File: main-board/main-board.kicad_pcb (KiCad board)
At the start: 2 copper layers, 180 x 111 mm, 53 parts, among them J1 INPUT, J2 NC1, J3 OUTPUT, J4 Conn_01x03_Pin, J5 COM, J6 Conn_01x03_Pin, SW1 SW_SPST, U1 ADA4898-2, U2 ADA4898-2, U3 AD633ANZ

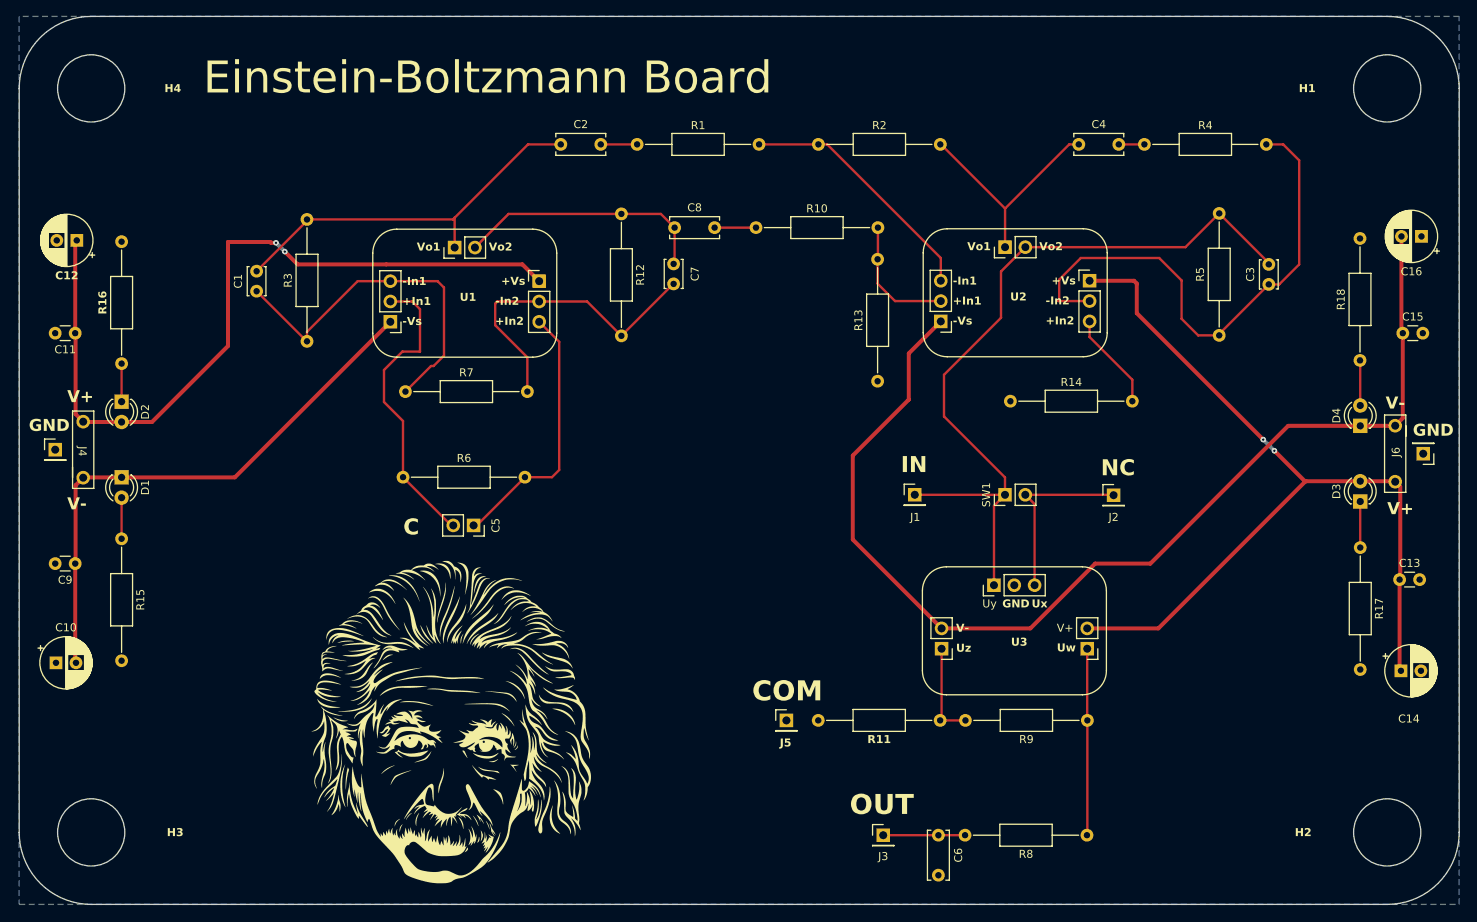
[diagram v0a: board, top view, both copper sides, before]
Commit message: Change M8 Holes to M5 Holes
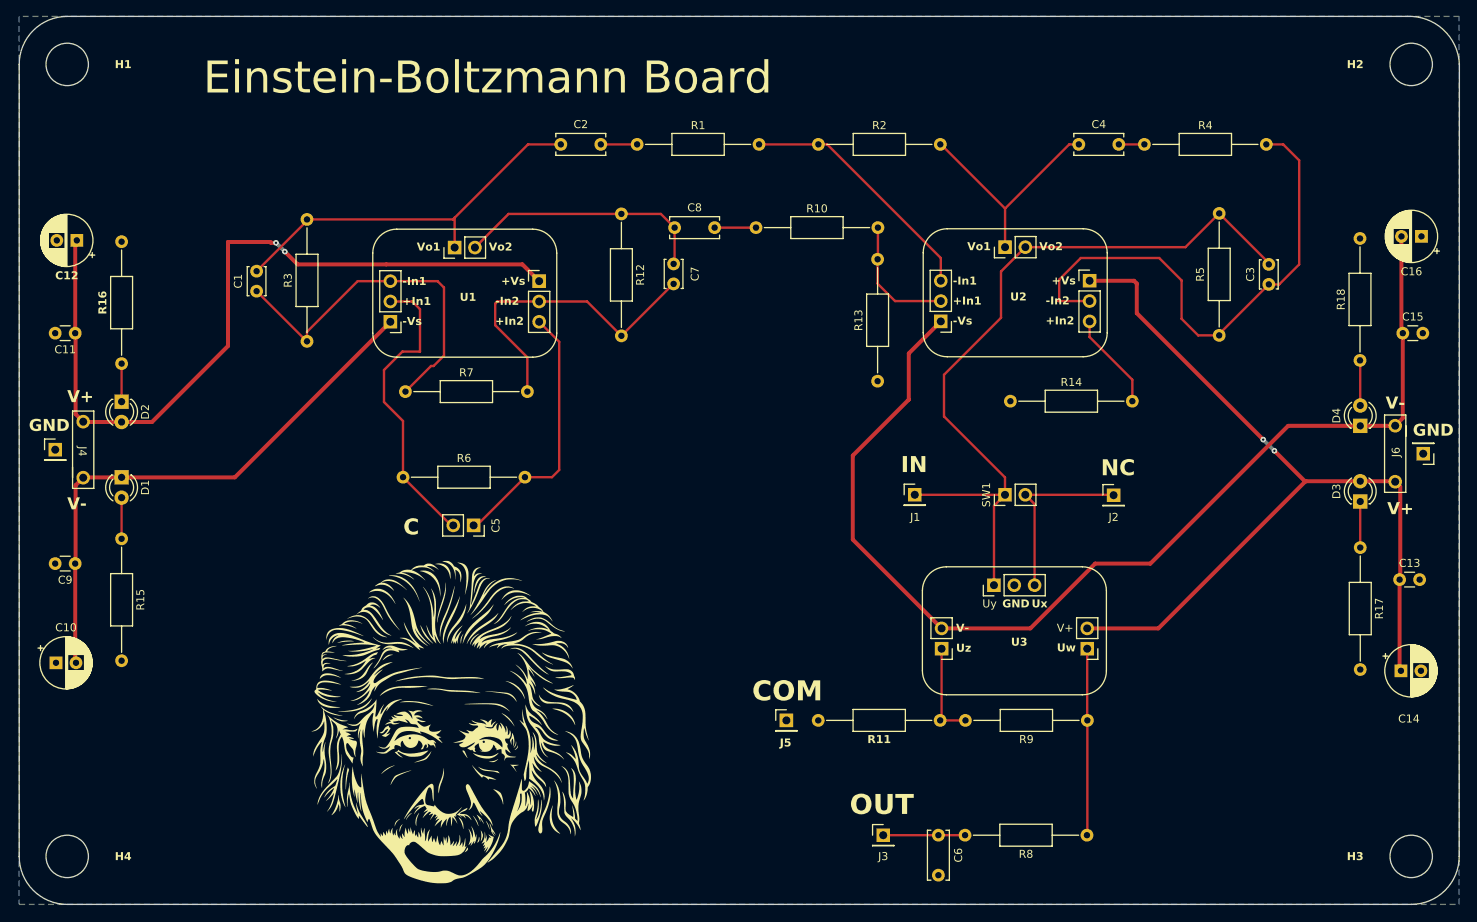
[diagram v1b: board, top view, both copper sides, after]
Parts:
- H1, H2, H3, H4: footprint MountingHole:MountingHole_8.4mm_M8 -> MountingHole:MountingHole_5.3mm_M5
- moved H1 165.0 mm to (66.0, 49.0)
- moved H3 165.0 mm to (234.0, 148.0)
- moved H2 96.0 mm to (234.0, 49.0)
- moved H4 96.0 mm to (66.0, 148.0)
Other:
- outline, holes or cut-outs redrawn

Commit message: Changes capacitor and resistor footprints
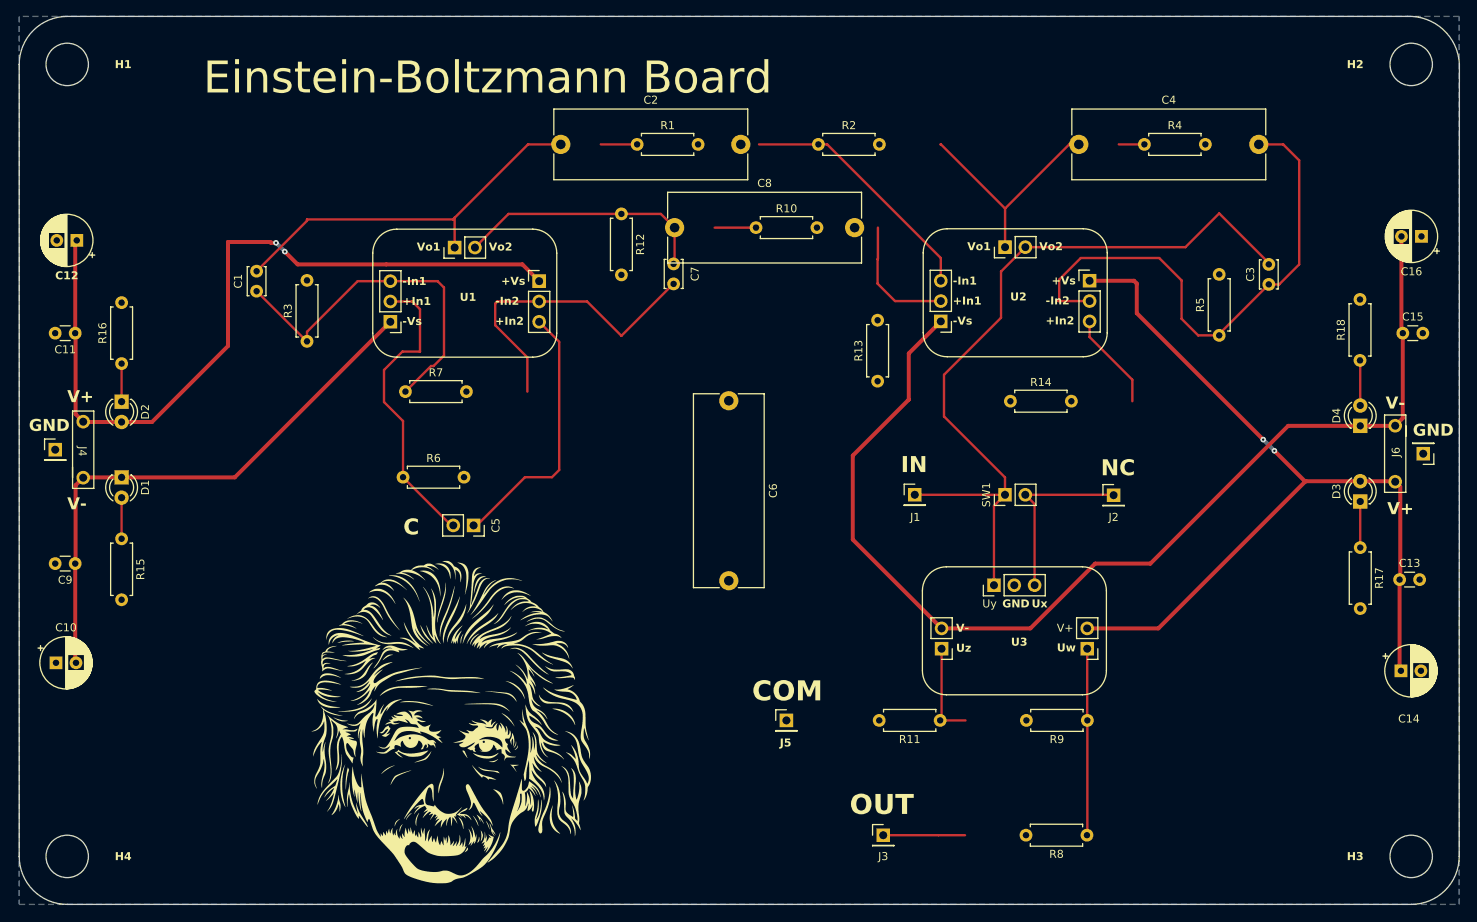
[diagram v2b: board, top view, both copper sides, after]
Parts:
- C2, C4, C6, C8: footprint Capacitor_THT:C_Disc_D6.0mm_W2.5mm_P5.00mm -> Capacitor_THT:C_Rect_L24.0mm_W8.6mm_P22.50mm_MKT
- R1, R10, R11, R12, R13, R14, R15, R16, R17, R18, R2, R3, R4, R5, R6, R7, R8, R9: footprint Resistor_THT:R_Axial_DIN0207_L6.3mm_D2.5mm_P15.24mm_Horizontal -> Resistor_THT:R_Axial_DIN0207_L6.3mm_D2.5mm_P7.62mm_Horizontal
- moved C6 60.3 mm to (148.7, 91.0)

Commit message: Saves progress
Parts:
- J1, J2, J3, J5: footprint Connector_PinHeader_2.54mm:PinHeader_1x01_P2.54mm_Vertical -> footprints:Banana_Jack_1Pin
- moved J1 96.2 mm to (84.4, 142.5)
- moved J3 84.5 mm to (85.8, 126.1)
- moved J2 26.6 mm to (213.6, 123.5)
- moved J5 18.0 mm to (140.0, 122.7)
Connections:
- C1 pad 2: /w3 -> VCC
- C2 pad 1: /w3 -> VCC
- U1 pad 4: /w3 -> VCC
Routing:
- net /w3: track 48.4 -> 0.00 mm
- net VCC: track 99.1 -> 146.0 mm, vias 2 -> 0
- net /w_out: track 10.2 -> 0.00 mm

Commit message: Adds Switch footprint and 3d model
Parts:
- added SW2: SW_Push_SPDT, footprints:Switch_Toggle_SPDT_SS12F46, F.Cu at (88.4, 104.4)
- added SW3: SW_Push_SPDT, footprints:Switch_Toggle_SPDT_SS12F46, F.Cu at (96.0, 104.4)
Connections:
- C1 pad 2: VCC -> /w3
- C2 pad 1: VCC -> /w3
- U1 pad 4: VCC -> /w3
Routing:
- net VCC: track 146.0 -> 97.6 mm
- net /w3: track 0.00 -> 48.4 mm

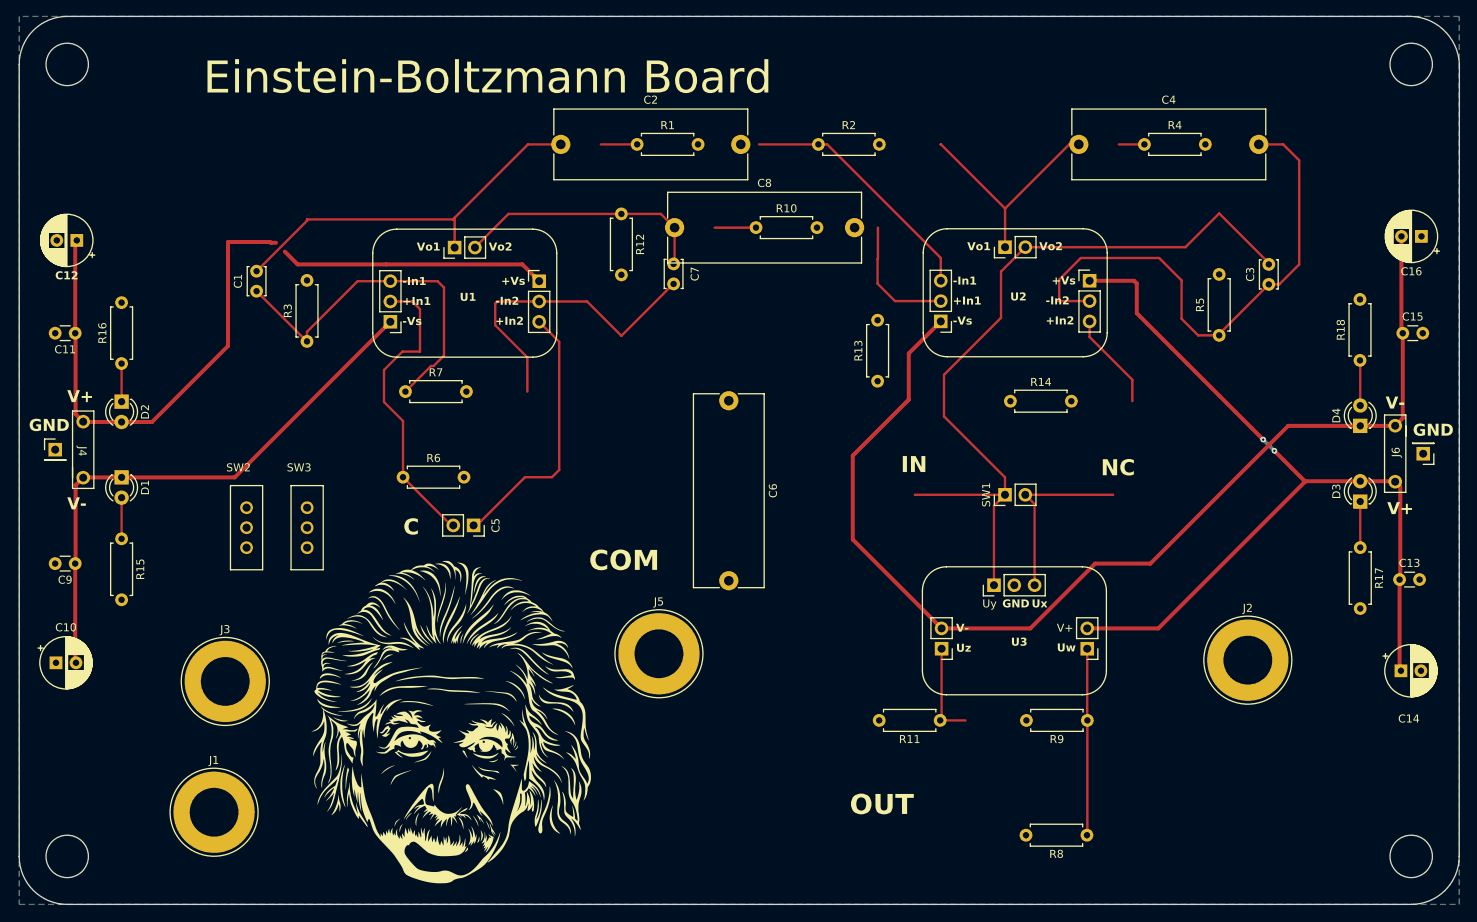
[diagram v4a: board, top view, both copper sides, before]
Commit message: Solves the 4 batteries problem
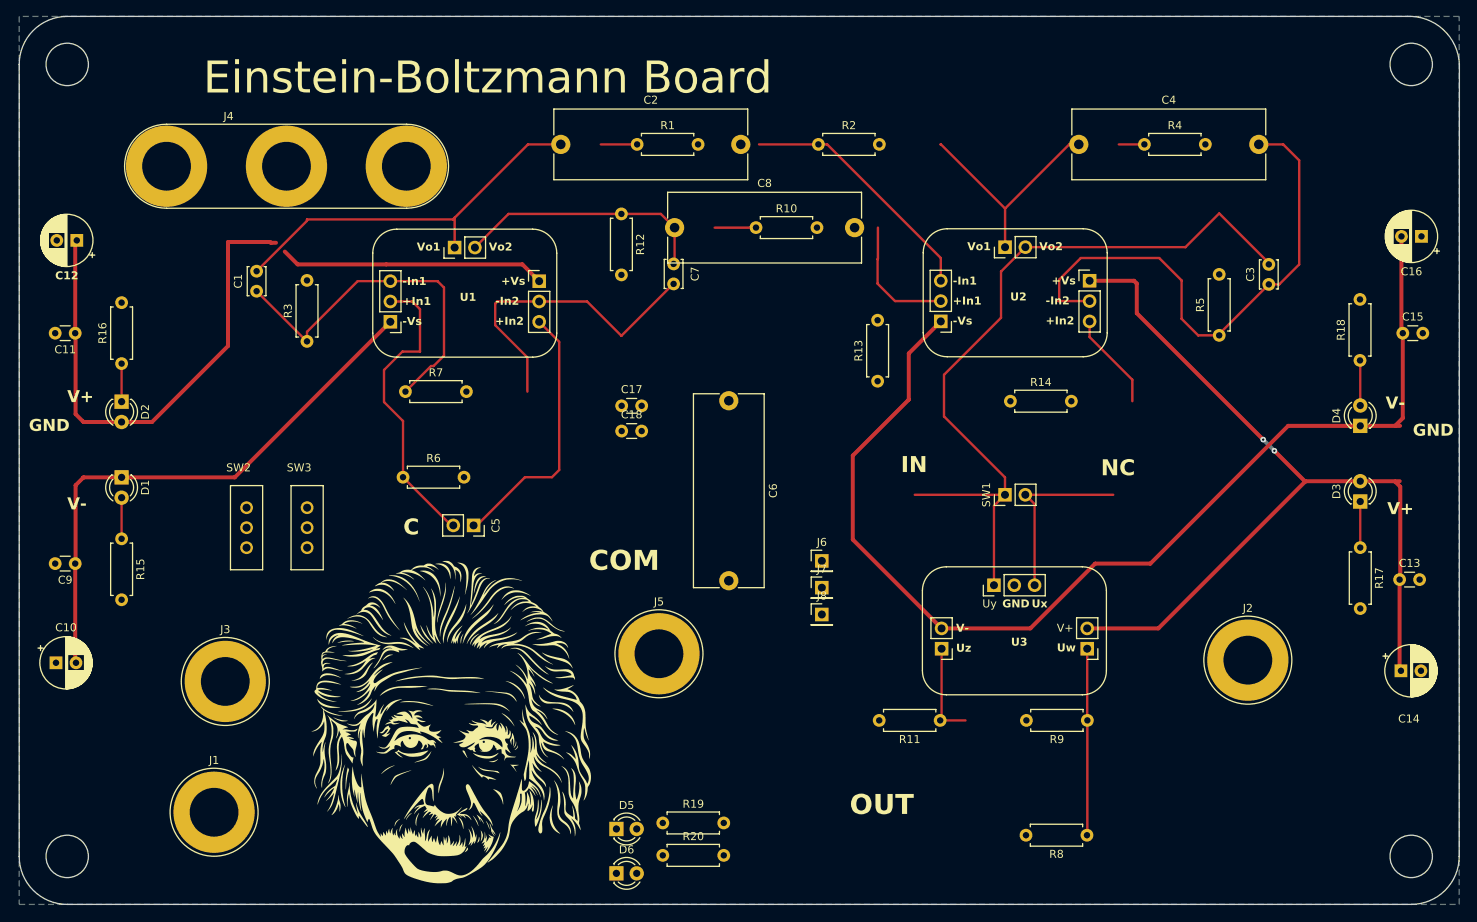
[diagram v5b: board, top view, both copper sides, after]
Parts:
- added C17: 0.1u, Capacitor_THT:C_Disc_D3.0mm_W1.6mm_P2.50mm, F.Cu at (135.3, 91.7)
- added C18: 0.1u, Capacitor_THT:C_Disc_D3.0mm_W1.6mm_P2.50mm, F.Cu at (135.3, 94.8)
- added D5: LED, LED_THT:LED_D3.0mm, F.Cu at (134.7, 144.6)
- added D6: LED, LED_THT:LED_D3.0mm, F.Cu at (134.7, 150.1)
- added J7: NC__DEBUG, Connector_PinHeader_2.54mm:PinHeader_1x01_P2.54mm_Vertical, F.Cu at (160.3, 114.4)
- added J8: OUTPUT_DEBUG, Connector_PinHeader_2.54mm:PinHeader_1x01_P2.54mm_Vertical, F.Cu at (160.3, 117.8)
- added R19: 2k, Resistor_THT:R_Axial_DIN0207_L6.3mm_D2.5mm_P7.62mm_Horizontal, F.Cu at (140.4, 143.8)
- added R20: 2k, Resistor_THT:R_Axial_DIN0207_L6.3mm_D2.5mm_P7.62mm_Horizontal, F.Cu at (140.4, 147.9)
- J4: footprint footprints:PowerHeader -> footprints:Banana_Jack_3Pin
- J6: value Conn_01x03_Pin -> INPUT_DEBUG; footprint footprints:PowerHeader -> Connector_PinHeader_2.54mm:PinHeader_1x01_P2.54mm_Vertical
- moved J6 73.6 mm to (160.3, 111.1), turned to 0 degrees
- moved J4 40.3 mm to (78.4, 61.7)
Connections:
- net /led_VCC renamed /led_+9V
- net /led_VDD renamed /led_+9VA
- net /led_VEE renamed /led_-9VA
- net /led_VSS renamed /led_-9V
- C10 pad 2: VSS -> -9VA
- C11 pad 1: VCC -> +9VA
- C12 pad 1: VCC -> +9VA
- C13 pad 1: VDD -> +9VB
- C14 pad 1: VDD -> +9VB
- C15 pad 1: VEE -> -9VB
- C16 pad 2: VEE -> -9VB
- C9 pad 1: VSS -> -9VA
- D1 pad 1: VSS -> -9V
- D2 pad 2: VCC -> +9V
- D3 pad 2: VDD -> +9VA
- D4 pad 1: VEE -> -9VA
- J4 pad 1: VSS -> +9V
- J4 pad 3: VCC -> -9V
- J6 pad 1: VEE -> /w_input
- U1 pad 1: VSS -> -9VA
- U1 pad 6: VCC -> +9VA
- U2 pad 1: VEE -> -9VB
- U2 pad 6: VDD -> +9VB
- U3 pad 2: VEE -> -9VB
- U3 pad 6: VDD -> +9VB
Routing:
- net (no net): track 0.00 -> 384.0 mm, vias 0 -> 2
- net VEE: track 139.5 -> 0.00 mm
- net VDD: track 110.2 -> 0.00 mm, vias 2 -> 0
- net VCC: track 97.6 -> 0.00 mm
- net VSS: track 70.1 -> 0.00 mm
- net +9VA: track 0.00 -> 33.3 mm

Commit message: Save changes
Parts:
- SW2: value SW_Push_SPDT -> Power Switch A; footprint footprints:Switch_Toggle_SPDT_SS12F46 -> footprints:SW_Push_2P2T_Toggle_CK_PSW-8,0R
- SW3: value SW_Push_SPDT -> Power Switch B; footprint footprints:Switch_Toggle_SPDT_SS12F46 -> footprints:SW_Push_2P2T_Toggle_CK_PSW-8,0R
- moved J3 114.9 mm to (199.0, 145.5)
- moved R17 85.4 mm to (170.4, 46.0)
- moved D3 66.3 mm to (178.5, 59.1)
- moved D4 64.0 mm to (180.2, 51.2)
- moved J8 57.6 mm to (216.6, 129.9)
- moved J7 38.9 mm to (197.5, 103.0)
- moved R8 38.6 mm to (228.8, 129.9)
- moved R11 34.5 mm to (208.6, 122.7)
- moved R9 34.5 mm to (227.0, 122.7)
- moved C13 33.2 mm to (199.3, 114.5)
- moved J2 22.1 mm to (212.0, 145.5), turned to 180 degrees
- moved J6 14.0 mm to (171.8, 103.0)
- moved SW3 13.3 mm to (83.3, 108.2)
- moved SW2 7.88 mm to (96.2, 103.2)
- moved U1 0.07 mm to (106.4, 81.3)
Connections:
- SW2 pad 1: unconnected-(SW2-A-Pad1) -> +9VA
- SW2 pad 2: unconnected-(SW2-B-Pad2) -> +9V
- SW3 pad 1: unconnected-(SW3-A-Pad1) -> +9VB
- SW3 pad 2: unconnected-(SW3-B-Pad2) -> +9V
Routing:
- net (no net): track 384.0 -> 0.00 mm, vias 2 -> 0
- net /w_input: track 96.2 -> 0.00 mm
- net /w12: track 66.1 -> 0.00 mm
- net /w3: track 48.4 -> 0.00 mm
- net /w1: track 45.4 -> 0.03 mm
- net /w2: track 39.5 -> 0.00 mm
- net /w_signal+: track 38.0 -> 0.00 mm
- net +9VA: track 33.3 -> 0.00 mm
- net /w_signal-: track 33.1 -> 0.00 mm
- net /w4: track 32.0 -> 0.00 mm
- net /w7: track 31.4 -> 0.00 mm
- net /w10: track 28.8 -> 0.00 mm
- net /w13: track 23.8 -> 0.00 mm
- net /w_nc: track 22.8 -> 0.00 mm
- net /w8: track 15.8 -> 0.00 mm
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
